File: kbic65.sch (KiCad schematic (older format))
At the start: 5 parts

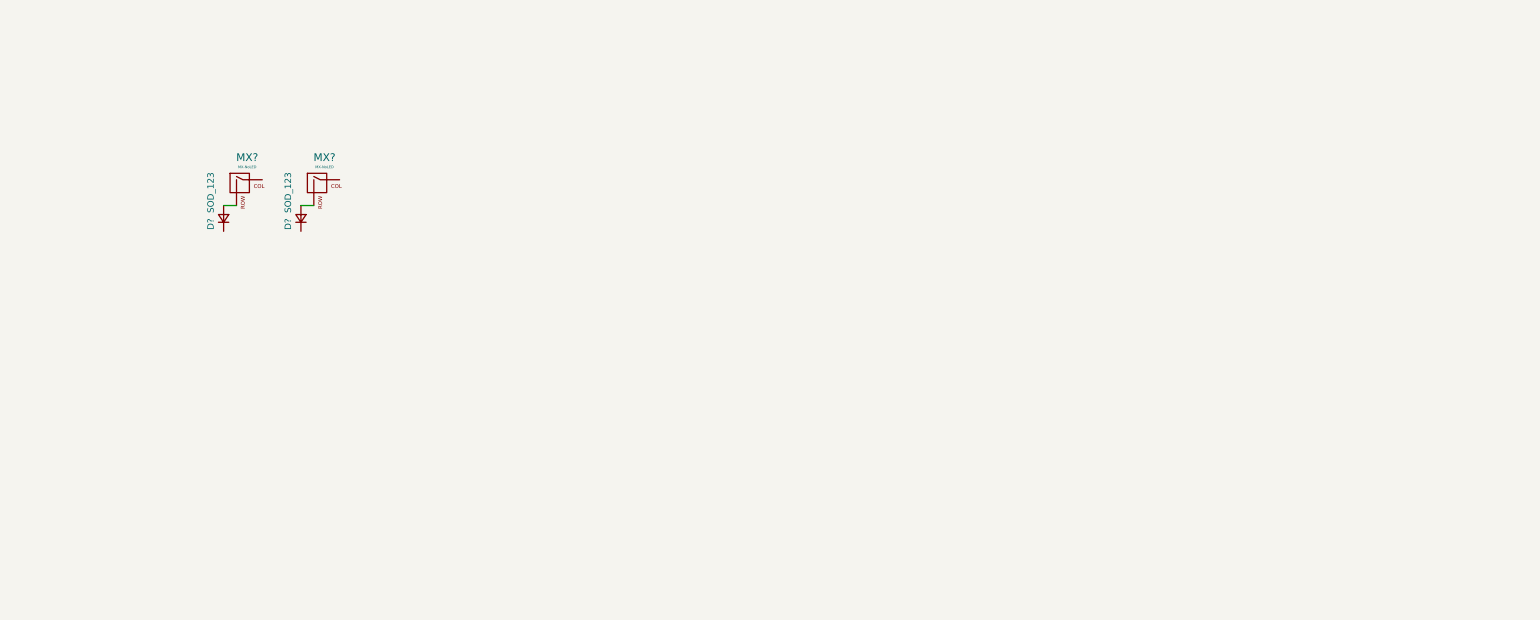
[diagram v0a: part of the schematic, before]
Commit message: Added key matrix
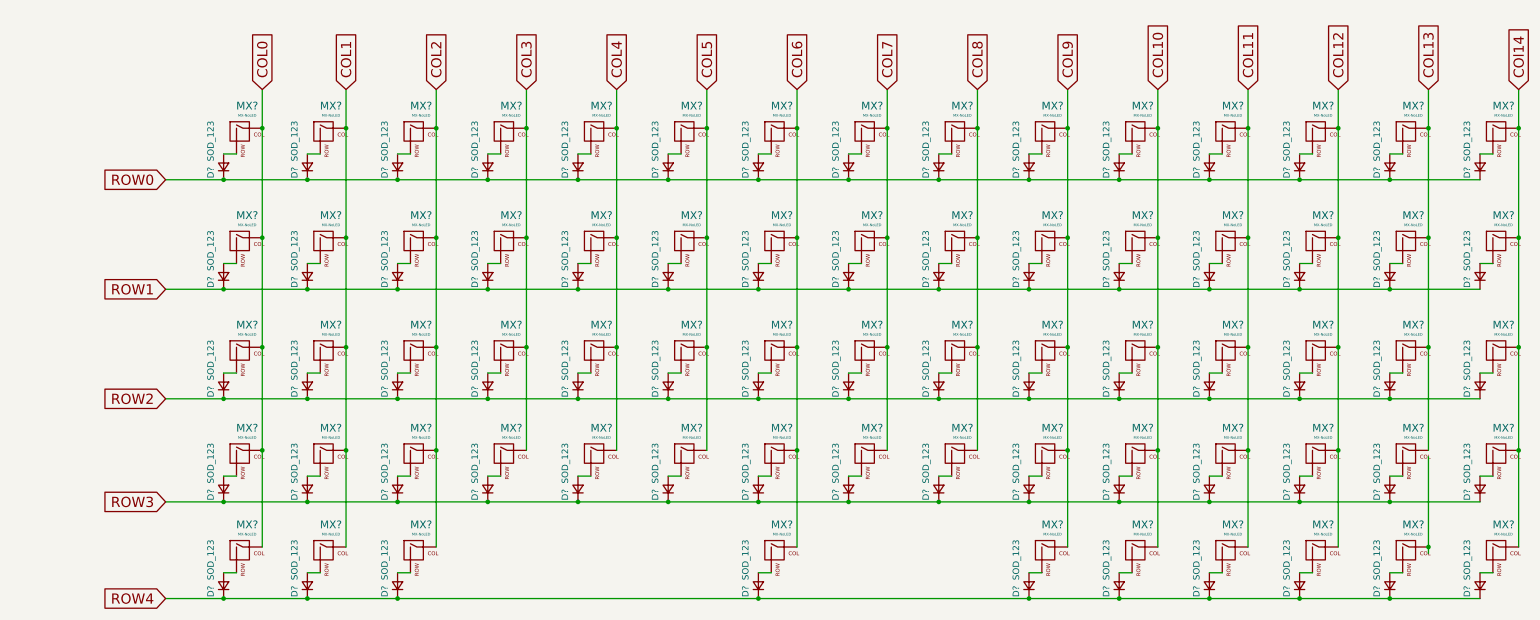
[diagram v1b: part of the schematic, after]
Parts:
- removed D?: SOD_123, symbol Device:D_Small
- removed MX?: MX-NoLED, symbol MX_Alps_Hybrid:MX-NoLED
- added D? (x69): SOD_123, symbol Device:D_Small
- added MX? (x69): MX-NoLED, symbol MX_Alps_Hybrid:MX-NoLED
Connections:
- net COL0: now reaches MX?.1 (COL)
- net COL0: now also MX?.1 (COL), MX?.1 (COL), MX?.1 (COL), MX?.1 (COL)
- net ROW0: now reaches D?.1 (K)
- net ROW0: now also D?.1 (K), D?.1 (K), D?.1 (K), D?.1 (K), D?.1 (K), D?.1 (K), D?.1 (K), D?.1 (K), D?.1 (K), D?.1 (K), D?.1 (K), D?.1 (K), D?.1 (K), D?.1 (K)
- new net: D?.2 (A), MX?.2 (ROW) (x69)
- new net COL1: MX?.1 (COL), MX?.1 (COL), MX?.1 (COL), MX?.1 (COL), MX?.1 (COL)
- new net COL10: MX?.1 (COL), MX?.1 (COL), MX?.1 (COL), MX?.1 (COL), MX?.1 (COL)
- new net COL11: MX?.1 (COL), MX?.1 (COL), MX?.1 (COL), MX?.1 (COL), MX?.1 (COL)
- new net COL12: MX?.1 (COL), MX?.1 (COL), MX?.1 (COL), MX?.1 (COL), MX?.1 (COL)
- new net COL13: MX?.1 (COL), MX?.1 (COL), MX?.1 (COL), MX?.1 (COL)
- new net COL2: MX?.1 (COL), MX?.1 (COL), MX?.1 (COL), MX?.1 (COL), MX?.1 (COL)
- new net COL3: MX?.1 (COL), MX?.1 (COL), MX?.1 (COL), MX?.1 (COL)
- new net COL4: MX?.1 (COL), MX?.1 (COL), MX?.1 (COL), MX?.1 (COL)
- new net COL5: MX?.1 (COL), MX?.1 (COL), MX?.1 (COL), MX?.1 (COL)
- new net COL6: MX?.1 (COL), MX?.1 (COL), MX?.1 (COL), MX?.1 (COL), MX?.1 (COL)
- new net COL7: MX?.1 (COL), MX?.1 (COL), MX?.1 (COL), MX?.1 (COL)
- new net COL8: MX?.1 (COL), MX?.1 (COL), MX?.1 (COL), MX?.1 (COL)
- new net COL9: MX?.1 (COL), MX?.1 (COL), MX?.1 (COL), MX?.1 (COL), MX?.1 (COL)
- new net COl14: MX?.1 (COL), MX?.1 (COL), MX?.1 (COL), MX?.1 (COL), MX?.1 (COL)
- new net ROW1: D?.1 (K), D?.1 (K), D?.1 (K), D?.1 (K), D?.1 (K), D?.1 (K), D?.1 (K), D?.1 (K), D?.1 (K), D?.1 (K), D?.1 (K), D?.1 (K), D?.1 (K), D?.1 (K), D?.1 (K)
- new net ROW2: D?.1 (K), D?.1 (K), D?.1 (K), D?.1 (K), D?.1 (K), D?.1 (K), D?.1 (K), D?.1 (K), D?.1 (K), D?.1 (K), D?.1 (K), D?.1 (K), D?.1 (K), D?.1 (K), D?.1 (K)
- new net ROW3: D?.1 (K), D?.1 (K), D?.1 (K), D?.1 (K), D?.1 (K), D?.1 (K), D?.1 (K), D?.1 (K), D?.1 (K), D?.1 (K), D?.1 (K), D?.1 (K), D?.1 (K), D?.1 (K), D?.1 (K)
- new net ROW4: D?.1 (K), D?.1 (K), D?.1 (K), D?.1 (K), D?.1 (K), D?.1 (K), D?.1 (K), D?.1 (K), D?.1 (K), D?.1 (K)
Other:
- moved on the sheet: D?, MX?

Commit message: Created new matrix and labeled ProMicro footprint
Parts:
- removed D? (x39): SOD_123, symbol Device:D_Small
- removed MX? (x39): MX-NoLED, symbol MX_Alps_Hybrid:MX-NoLED
- added D? (x39): SOD_123, symbol Device:D_Small
- added MX? (x39): MX-NoLED, symbol MX_Alps_Hybrid:MX-NoLED
- added U?: ProMicro, symbol promicro:ProMicro
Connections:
- net COL0: now also U?.20 (F4), MX?.1 (COL), MX?.1 (COL), MX?.1 (COL), MX?.1 (COL), MX?.1 (COL), U?.20 (F4)
- net COL1: now also U?.19 (F5), MX?.1 (COL), MX?.1 (COL), MX?.1 (COL), MX?.1 (COL), MX?.1 (COL), U?.19 (F5)
- net COL2: now also U?.18 (F6), MX?.1 (COL), MX?.1 (COL), MX?.1 (COL), MX?.1 (COL), MX?.1 (COL), U?.18 (F6)
- net COL3: now also U?.17 (F7), MX?.1 (COL), MX?.1 (COL), MX?.1 (COL), MX?.1 (COL), MX?.1 (COL), U?.17 (F7)
- net COL4: now also U?.16 (B1), MX?.1 (COL), MX?.1 (COL), MX?.1 (COL), MX?.1 (COL), MX?.1 (COL), U?.16 (B1)
- net COL5: now also U?.15 (B3), MX?.1 (COL), MX?.1 (COL), MX?.1 (COL), MX?.1 (COL), MX?.1 (COL), U?.15 (B3)
- net COL6: now also U?.14 (B2), MX?.1 (COL), MX?.1 (COL), MX?.1 (COL), MX?.1 (COL), U?.14 (B2)
- net COL7: now also U?.13 (B6), MX?.1 (COL), MX?.1 (COL), MX?.1 (COL), MX?.1 (COL), MX?.1 (COL), U?.13 (B6)
- net ROW0: now also U?.1 (TX), U?.2 (RX)
- net ROW1: now also U?.2 (RX), U?.5 (SCL)
- net ROW2: now also U?.5 (SCL), U?.6 (SDA)
- net ROW3: now also U?.6 (SDA), U?.7 (D4)
- net ROW4: now also U?.7 (D4), D?.1 (K), D?.1 (K), D?.1 (K), D?.1 (K), D?.1 (K), D?.1 (K), D?.1 (K), U?.8 (C6)
- net ROW7: now reaches U?.10 (E6)
- net ROW7: now also D?.1 (K), D?.1 (K), D?.1 (K), D?.1 (K), D?.1 (K), D?.1 (K), D?.1 (K), D?.1 (K), U?.11 (B4)
- net ROW8: now reaches U?.11 (B4)
- net ROW8: now also D?.1 (K), D?.1 (K), D?.1 (K), D?.1 (K), D?.1 (K), D?.1 (K), D?.1 (K), D?.1 (K), U?.12 (B5)
- net ROW5: now reaches U?.8 (C6)
- net ROW5: now also D?.1 (K), D?.1 (K), D?.1 (K), D?.1 (K), D?.1 (K), D?.1 (K), D?.1 (K), D?.1 (K), U?.9 (D7)
- net ROW6: now reaches U?.9 (D7)
- net ROW6: now also D?.1 (K), D?.1 (K), D?.1 (K), D?.1 (K), D?.1 (K), D?.1 (K), D?.1 (K), D?.1 (K), U?.10 (E6)
- new net: D?.2 (A), MX?.2 (ROW) (x39)
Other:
- moved on the sheet: D?, MX?

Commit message: Naming matrix components
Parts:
- removed U?: ProMicro, symbol promicro:ProMicro
- gave numbers to parts that had none: 50
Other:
- moved on the sheet: U?

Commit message: Naming matrix components
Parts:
- gave numbers to parts that had none: 90
- renumbered MX_; to MX_SemiCol

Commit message: Added footprints
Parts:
- D_0, D_1, D_2, D_3, D_4, D_5, D_6, D_7, D_8, D_9, D_BkSp1, D_BkSp2: footprint (none) -> Diode_THT:D_DO-35_SOD27_P5.08mm_Vertical_AnodeUp
- D_@1: renamed from D_@; footprint (none) -> Diode_THT:D_DO-35_SOD27_P5.08mm_Vertical_AnodeUp
- D_A1: renamed from D_A; footprint (none) -> Diode_THT:D_DO-35_SOD27_P5.08mm_Vertical_AnodeUp
- D_B1: renamed from D_B; footprint (none) -> Diode_THT:D_DO-35_SOD27_P5.08mm_Vertical_AnodeUp
- D_BKSLSH1: renamed from D_BKSLSH; footprint (none) -> Diode_THT:D_DO-35_SOD27_P5.08mm_Vertical_AnodeUp
- D_C1: renamed from D_C; footprint (none) -> Diode_THT:D_DO-35_SOD27_P5.08mm_Vertical_AnodeUp
- D_Comma1: renamed from D_Comma; footprint (none) -> Diode_THT:D_DO-35_SOD27_P5.08mm_Vertical_AnodeUp
- D_CpsLck1: renamed from D_CpsLck; footprint (none) -> Diode_THT:D_DO-35_SOD27_P5.08mm_Vertical_AnodeUp
- D_D1: renamed from D_D; footprint (none) -> Diode_THT:D_DO-35_SOD27_P5.08mm_Vertical_AnodeUp
- D_Del1: renamed from D_Del; footprint (none) -> Diode_THT:D_DO-35_SOD27_P5.08mm_Vertical_AnodeUp
- D_Dot1: renamed from D_Dot; footprint (none) -> Diode_THT:D_DO-35_SOD27_P5.08mm_Vertical_AnodeUp
- D_Down1: renamed from D_Down; footprint (none) -> Diode_THT:D_DO-35_SOD27_P5.08mm_Vertical_AnodeUp
- D_E1: renamed from D_E; footprint (none) -> Diode_THT:D_DO-35_SOD27_P5.08mm_Vertical_AnodeUp
- D_Enter1: renamed from D_Enter; footprint (none) -> Diode_THT:D_DO-35_SOD27_P5.08mm_Vertical_AnodeUp
- D_Equal1: renamed from D_Equal; footprint (none) -> Diode_THT:D_DO-35_SOD27_P5.08mm_Vertical_AnodeUp
- D_Esc1: renamed from D_Esc; footprint (none) -> Diode_THT:D_DO-35_SOD27_P5.08mm_Vertical_AnodeUp
- D_F1: renamed from D_F; footprint (none) -> Diode_THT:D_DO-35_SOD27_P5.08mm_Vertical_AnodeUp
- D_FwdSlsh1: renamed from D_FwdSlsh; footprint (none) -> Diode_THT:D_DO-35_SOD27_P5.08mm_Vertical_AnodeUp
- D_G1: renamed from D_G; footprint (none) -> Diode_THT:D_DO-35_SOD27_P5.08mm_Vertical_AnodeUp
- D_H1: renamed from D_H; footprint (none) -> Diode_THT:D_DO-35_SOD27_P5.08mm_Vertical_AnodeUp
- D_Hyphen1: renamed from D_Hyphen; footprint (none) -> Diode_THT:D_DO-35_SOD27_P5.08mm_Vertical_AnodeUp
- D_I1: renamed from D_I; footprint (none) -> Diode_THT:D_DO-35_SOD27_P5.08mm_Vertical_AnodeUp
- D_ISO_BKSLSH1: renamed from D_ISO_BKSLSH; footprint (none) -> Diode_THT:D_DO-35_SOD27_P5.08mm_Vertical_AnodeUp
- D_J1: renamed from D_J; footprint (none) -> Diode_THT:D_DO-35_SOD27_P5.08mm_Vertical_AnodeUp
- D_K1: renamed from D_K; footprint (none) -> Diode_THT:D_DO-35_SOD27_P5.08mm_Vertical_AnodeUp
- D_L1: renamed from D_L; footprint (none) -> Diode_THT:D_DO-35_SOD27_P5.08mm_Vertical_AnodeUp
- D_LAlt1: renamed from D_LAlt; footprint (none) -> Diode_THT:D_DO-35_SOD27_P5.08mm_Vertical_AnodeUp
- D_LBKT1: renamed from D_LBKT; footprint (none) -> Diode_THT:D_DO-35_SOD27_P5.08mm_Vertical_AnodeUp
- D_LCtrl1: renamed from D_LCtrl; footprint (none) -> Diode_THT:D_DO-35_SOD27_P5.08mm_Vertical_AnodeUp
- D_LShift1: renamed from D_LShift; footprint (none) -> Diode_THT:D_DO-35_SOD27_P5.08mm_Vertical_AnodeUp
- D_LWin1: renamed from D_LWin; footprint (none) -> Diode_THT:D_DO-35_SOD27_P5.08mm_Vertical_AnodeUp
- D_Left1: renamed from D_Left; footprint (none) -> Diode_THT:D_DO-35_SOD27_P5.08mm_Vertical_AnodeUp
- D_M1: renamed from D_M; footprint (none) -> Diode_THT:D_DO-35_SOD27_P5.08mm_Vertical_AnodeUp
- D_N1: renamed from D_N; footprint (none) -> Diode_THT:D_DO-35_SOD27_P5.08mm_Vertical_AnodeUp
- D_O1: renamed from D_O; footprint (none) -> Diode_THT:D_DO-35_SOD27_P5.08mm_Vertical_AnodeUp
- D_P1: renamed from D_P; footprint (none) -> Diode_THT:D_DO-35_SOD27_P5.08mm_Vertical_AnodeUp
- D_PgDn1: renamed from D_PgDn; footprint (none) -> Diode_THT:D_DO-35_SOD27_P5.08mm_Vertical_AnodeUp
- D_PgUp1: renamed from D_PgUp; footprint (none) -> Diode_THT:D_DO-35_SOD27_P5.08mm_Vertical_AnodeUp
- D_Q1: renamed from D_Q; footprint (none) -> Diode_THT:D_DO-35_SOD27_P5.08mm_Vertical_AnodeUp
- D_R1: renamed from D_R; footprint (none) -> Diode_THT:D_DO-35_SOD27_P5.08mm_Vertical_AnodeUp
- D_RAlt1: renamed from D_RAlt; footprint (none) -> Diode_THT:D_DO-35_SOD27_P5.08mm_Vertical_AnodeUp
- D_RBKT1: renamed from D_RBKT; footprint (none) -> Diode_THT:D_DO-35_SOD27_P5.08mm_Vertical_AnodeUp
- D_RCtrl1: renamed from D_RCtrl; footprint (none) -> Diode_THT:D_DO-35_SOD27_P5.08mm_Vertical_AnodeUp
- D_RShift1: renamed from D_RShift; footprint (none) -> Diode_THT:D_DO-35_SOD27_P5.08mm_Vertical_AnodeUp
- D_RWin1: renamed from D_RWin; footprint (none) -> Diode_THT:D_DO-35_SOD27_P5.08mm_Vertical_AnodeUp
- D_Right1: renamed from D_Right; footprint (none) -> Diode_THT:D_DO-35_SOD27_P5.08mm_Vertical_AnodeUp
- D_S1: renamed from D_S; footprint (none) -> Diode_THT:D_DO-35_SOD27_P5.08mm_Vertical_AnodeUp
- D_SemiCol1: renamed from D_SemiCol; footprint (none) -> Diode_THT:D_DO-35_SOD27_P5.08mm_Vertical_AnodeUp
- D_Space1: renamed from D_Space; footprint (none) -> Diode_THT:D_DO-35_SOD27_P5.08mm_Vertical_AnodeUp
- D_T1: renamed from D_T; footprint (none) -> Diode_THT:D_DO-35_SOD27_P5.08mm_Vertical_AnodeUp
- D_Tab1: renamed from D_Tab; footprint (none) -> Diode_THT:D_DO-35_SOD27_P5.08mm_Vertical_AnodeUp
- D_Tilde1: renamed from D_Tilde; footprint (none) -> Diode_THT:D_DO-35_SOD27_P5.08mm_Vertical_AnodeUp
- D_U1: renamed from D_U; footprint (none) -> Diode_THT:D_DO-35_SOD27_P5.08mm_Vertical_AnodeUp
- D_Up1: renamed from D_Up; footprint (none) -> Diode_THT:D_DO-35_SOD27_P5.08mm_Vertical_AnodeUp
- D_V1: renamed from D_V; footprint (none) -> Diode_THT:D_DO-35_SOD27_P5.08mm_Vertical_AnodeUp
- D_W1: renamed from D_W; footprint (none) -> Diode_THT:D_DO-35_SOD27_P5.08mm_Vertical_AnodeUp
- D_X1: renamed from D_X; footprint (none) -> Diode_THT:D_DO-35_SOD27_P5.08mm_Vertical_AnodeUp
- D_Y1: renamed from D_Y; footprint (none) -> Diode_THT:D_DO-35_SOD27_P5.08mm_Vertical_AnodeUp
- D_Z1: renamed from D_Z; footprint (none) -> Diode_THT:D_DO-35_SOD27_P5.08mm_Vertical_AnodeUp
- MX_0, MX_1, MX_2, MX_3, MX_4, MX_5, MX_6, MX_7, MX_8, MX_9, MX_BkSp1, MX_BkSp2: footprint (none) -> MX_Alps_Hybrid:MX-1U-NoLED
- MX_@1: renamed from MX_@; footprint (none) -> MX_Alps_Hybrid:MX-1U-NoLED
- MX_A1: renamed from MX_A; footprint (none) -> MX_Alps_Hybrid:MX-1U-NoLED
- MX_B1: renamed from MX_B; footprint (none) -> MX_Alps_Hybrid:MX-1U-NoLED
- MX_BKSLSH1: renamed from MX_BKSLSH; footprint (none) -> MX_Alps_Hybrid:MX-1U-NoLED
- MX_C1: renamed from MX_C; footprint (none) -> MX_Alps_Hybrid:MX-1U-NoLED
- MX_Comma1: renamed from MX_Comma; footprint (none) -> MX_Alps_Hybrid:MX-1U-NoLED
- MX_CpsLck1: renamed from MX_CpsLck; footprint (none) -> MX_Alps_Hybrid:MX-1U-NoLED
- MX_D1: renamed from MX_D; footprint (none) -> MX_Alps_Hybrid:MX-1U-NoLED
- MX_Del1: renamed from MX_Del; footprint (none) -> MX_Alps_Hybrid:MX-1U-NoLED
- MX_Dot1: renamed from MX_Dot; footprint (none) -> MX_Alps_Hybrid:MX-1U-NoLED
- MX_Down1: renamed from MX_Down; footprint (none) -> MX_Alps_Hybrid:MX-1U-NoLED
- MX_E1: renamed from MX_E; footprint (none) -> MX_Alps_Hybrid:MX-1U-NoLED
- MX_Enter1: renamed from MX_Enter; footprint (none) -> MX_Alps_Hybrid:MX-1U-NoLED
- MX_Equal1: renamed from MX_Equal; footprint (none) -> MX_Alps_Hybrid:MX-1U-NoLED
- MX_Esc1: renamed from MX_Esc; footprint (none) -> MX_Alps_Hybrid:MX-1U-NoLED
- MX_F1: renamed from MX_F; footprint (none) -> MX_Alps_Hybrid:MX-1U-NoLED
- MX_FwdSlsh1: renamed from MX_FwdSlsh; footprint (none) -> MX_Alps_Hybrid:MX-1U-NoLED
- MX_G1: renamed from MX_G; footprint (none) -> MX_Alps_Hybrid:MX-1U-NoLED
- MX_H1: renamed from MX_H; footprint (none) -> MX_Alps_Hybrid:MX-1U-NoLED
- MX_Hyphen1: renamed from MX_Hyphen; footprint (none) -> MX_Alps_Hybrid:MX-1U-NoLED
- MX_I1: renamed from MX_I; footprint (none) -> MX_Alps_Hybrid:MX-1U-NoLED
- MX_ISO_BKSLSH1: renamed from MX_ISO_BKSLSH; footprint (none) -> MX_Alps_Hybrid:MX-1U-NoLED
- MX_J1: renamed from MX_J; footprint (none) -> MX_Alps_Hybrid:MX-1U-NoLED
- MX_K1: renamed from MX_K; footprint (none) -> MX_Alps_Hybrid:MX-1U-NoLED
- MX_L1: renamed from MX_L; footprint (none) -> MX_Alps_Hybrid:MX-1U-NoLED
- MX_LAlt1: renamed from MX_LAlt; footprint (none) -> MX_Alps_Hybrid:MX-1U-NoLED
- MX_LBKT1: renamed from MX_LBKT; footprint (none) -> MX_Alps_Hybrid:MX-1U-NoLED
- MX_LCtrl1: renamed from MX_LCtrl; footprint (none) -> MX_Alps_Hybrid:MX-1U-NoLED
- MX_LShift1: renamed from MX_LShift; footprint (none) -> MX_Alps_Hybrid:MX-1U-NoLED
- MX_LWin1: renamed from MX_LWin; footprint (none) -> MX_Alps_Hybrid:MX-1U-NoLED
- MX_Left1: renamed from MX_Left; footprint (none) -> MX_Alps_Hybrid:MX-1U-NoLED
- MX_M1: renamed from MX_M; footprint (none) -> MX_Alps_Hybrid:MX-1U-NoLED
- MX_N1: renamed from MX_N; footprint (none) -> MX_Alps_Hybrid:MX-1U-NoLED
- MX_O1: renamed from MX_O; footprint (none) -> MX_Alps_Hybrid:MX-1U-NoLED
- MX_P1: renamed from MX_P; footprint (none) -> MX_Alps_Hybrid:MX-1U-NoLED
- MX_PgDn1: renamed from MX_PgDn; footprint (none) -> MX_Alps_Hybrid:MX-1U-NoLED
- MX_PgUp1: renamed from MX_PgUp; footprint (none) -> MX_Alps_Hybrid:MX-1U-NoLED
- MX_Q1: renamed from MX_Q; footprint (none) -> MX_Alps_Hybrid:MX-1U-NoLED
- MX_R1: renamed from MX_R; footprint (none) -> MX_Alps_Hybrid:MX-1U-NoLED
- MX_RAlt1: renamed from MX_RAlt; footprint (none) -> MX_Alps_Hybrid:MX-1U-NoLED
- MX_RBKT1: renamed from MX_RBKT; footprint (none) -> MX_Alps_Hybrid:MX-1U-NoLED
- MX_RCtrl1: renamed from MX_RCtrl; footprint (none) -> MX_Alps_Hybrid:MX-1U-NoLED
- MX_RShift1: renamed from MX_RShift; footprint (none) -> MX_Alps_Hybrid:MX-1U-NoLED
- MX_RWin1: renamed from MX_RWin; footprint (none) -> MX_Alps_Hybrid:MX-1U-NoLED
- MX_Right1: renamed from MX_Right; footprint (none) -> MX_Alps_Hybrid:MX-1U-NoLED
- MX_S1: renamed from MX_S; footprint (none) -> MX_Alps_Hybrid:MX-1U-NoLED
- MX_SemiCol1: renamed from MX_SemiCol; footprint (none) -> MX_Alps_Hybrid:MX-1U-NoLED
- MX_Space1: renamed from MX_Space; footprint (none) -> MX_Alps_Hybrid:MX-1U-NoLED
- MX_T1: renamed from MX_T; footprint (none) -> MX_Alps_Hybrid:MX-1U-NoLED
- MX_Tab1: renamed from MX_Tab; footprint (none) -> MX_Alps_Hybrid:MX-1U-NoLED
- MX_Tilde1: renamed from MX_Tilde; footprint (none) -> MX_Alps_Hybrid:MX-1U-NoLED
- MX_U1: renamed from MX_U; footprint (none) -> MX_Alps_Hybrid:MX-1U-NoLED
- MX_Up1: renamed from MX_Up; footprint (none) -> MX_Alps_Hybrid:MX-1U-NoLED
- MX_V1: renamed from MX_V; footprint (none) -> MX_Alps_Hybrid:MX-1U-NoLED
- MX_W1: renamed from MX_W; footprint (none) -> MX_Alps_Hybrid:MX-1U-NoLED
- MX_X1: renamed from MX_X; footprint (none) -> MX_Alps_Hybrid:MX-1U-NoLED
- MX_Y1: renamed from MX_Y; footprint (none) -> MX_Alps_Hybrid:MX-1U-NoLED
- MX_Z1: renamed from MX_Z; footprint (none) -> MX_Alps_Hybrid:MX-1U-NoLED
- U1: renamed from U?; footprint (none) -> Keebio-Parts:ArduinoProMicro-ZigZag

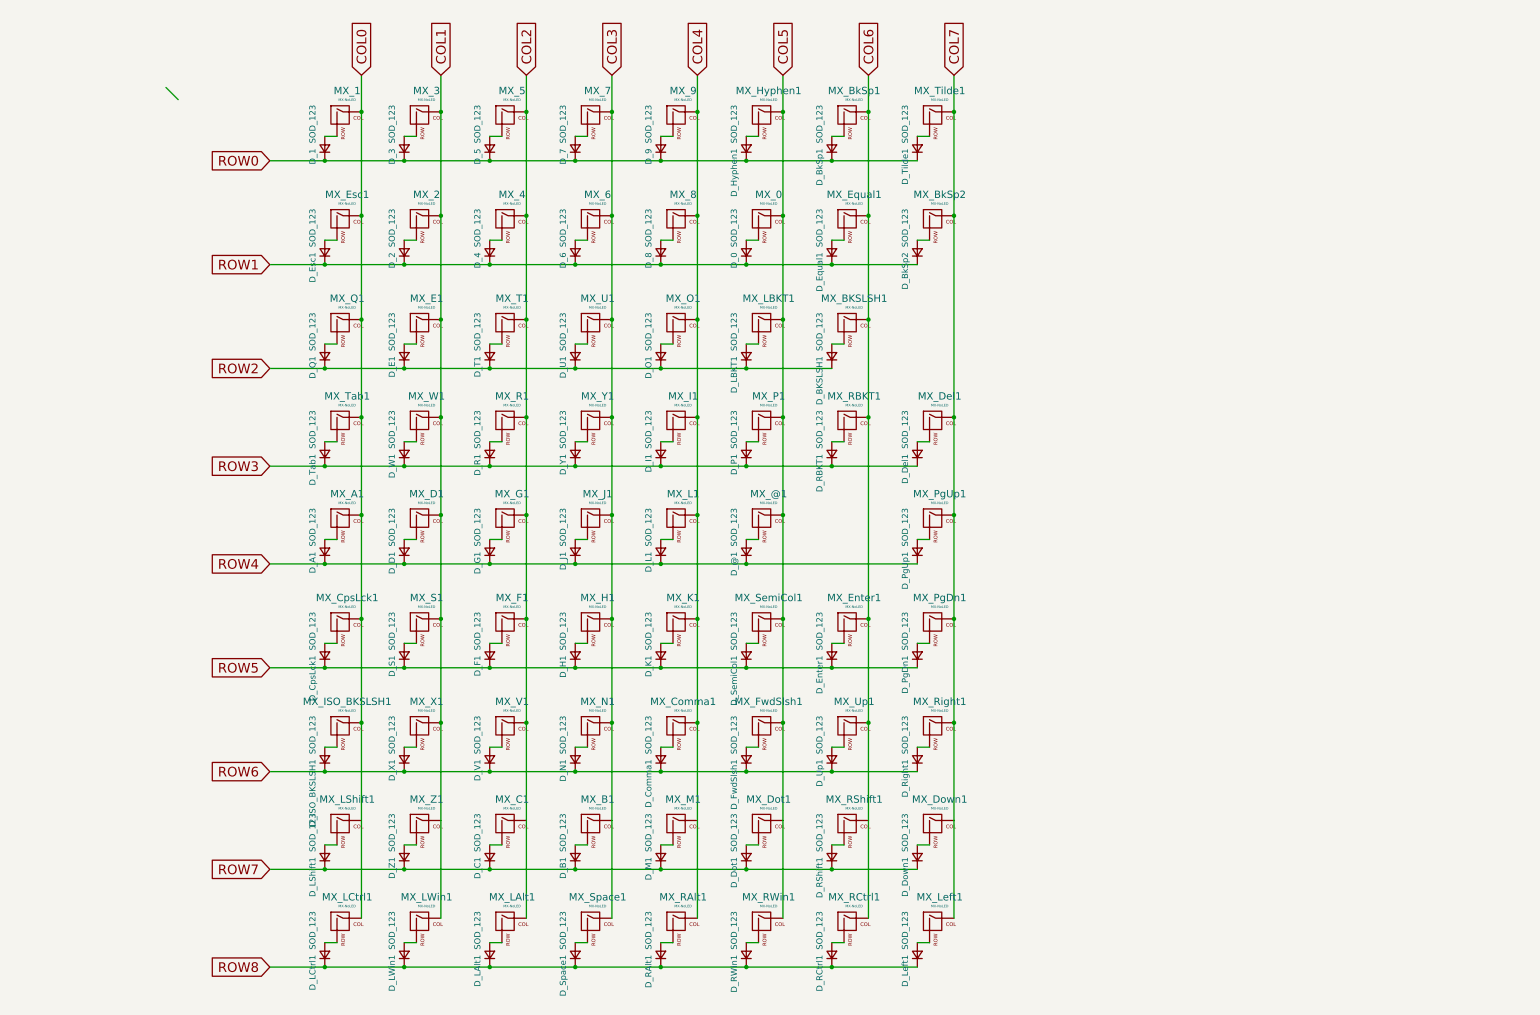
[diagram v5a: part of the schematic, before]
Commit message: Placed components on PCB and imported dxf
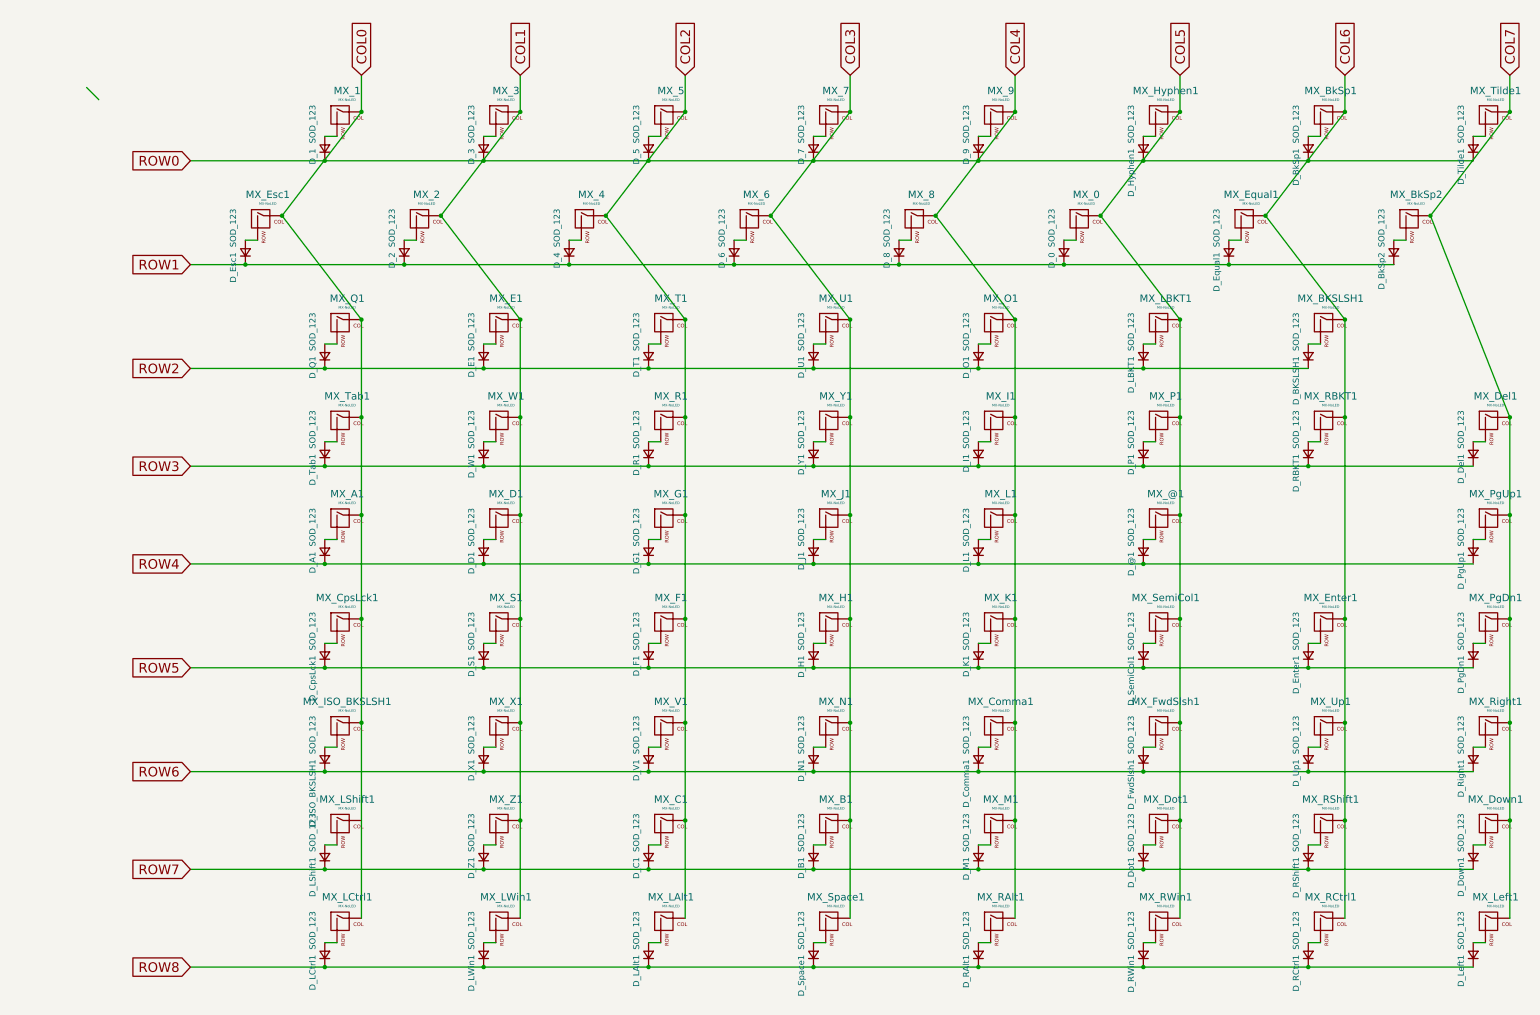
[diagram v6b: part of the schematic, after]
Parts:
- MX_0, MX_1, MX_2, MX_3, MX_4, MX_5, MX_6, MX_7, MX_8, MX_9, MX_@1, MX_A1, MX_B1, MX_BKSLSH1, MX_BkSp1, MX_BkSp2, MX_C1, MX_Comma1, MX_CpsLck1, MX_D1, MX_Del1, MX_Dot1, MX_Down1, MX_E1, MX_Enter1, MX_Equal1, MX_Esc1, MX_F1, MX_FwdSlsh1, MX_G1, MX_H1, MX_Hyphen1, MX_I1, MX_ISO_BKSLSH1, MX_J1, MX_K1, MX_L1, MX_LAlt1, MX_LBKT1, MX_LCtrl1, MX_LShift1, MX_LWin1, MX_Left1, MX_M1, MX_N1, MX_O1, MX_P1, MX_PgDn1, MX_PgUp1, MX_Q1, MX_R1, MX_RAlt1, MX_RBKT1, MX_RCtrl1, MX_RShift1, MX_RWin1, MX_Right1, MX_S1, MX_SemiCol1, MX_Space1, MX_T1, MX_Tab1, MX_Tilde1, MX_U1, MX_Up1, MX_V1, MX_W1, MX_X1, MX_Y1, MX_Z1: footprint MX_Alps_Hybrid:MX-1U-NoLED -> MX_Only:MXOnly-1U-NoLED
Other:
- moved on the sheet: D_0, D_3, D_4, D_5, D_6, D_7, D_8, D_9, D_@1, D_B1, D_BKSLSH1, D_BkSp1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
